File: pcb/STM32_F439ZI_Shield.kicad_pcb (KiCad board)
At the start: 2 copper layers, 70 x 133.4 mm, 112 parts, among them CN10 Conn_02x17_Odd_Even, CN7 Conn_02x10_Odd_Even, CN8 Conn_02x08_Odd_Even, CN9 Conn_02x15_Odd_Even, J1 Conn_01x02_Pin, J3 Relais_Conn, J4 Conn_01x02_Pin, J5 Conn_01x02_Pin, J6 Conn_01x02_Pin, J7 Conn_01x02_Pin, J8 Conn_01x02_Pin, K1 G6S-2, K2 G6S-2, U1 LM2904, U10 LTV-817S, U11 LTV-817S, U13 R-78E-5.0-1.0, U15 ACS724xLCTR-05AB, U2 MAX3485, U3 LTV-817S, U4 LTV-817S, U5 LTV-817S, U6 LTV-817S, U7 LTV-817S, U8 LTV-817S, U9 LTV-817S

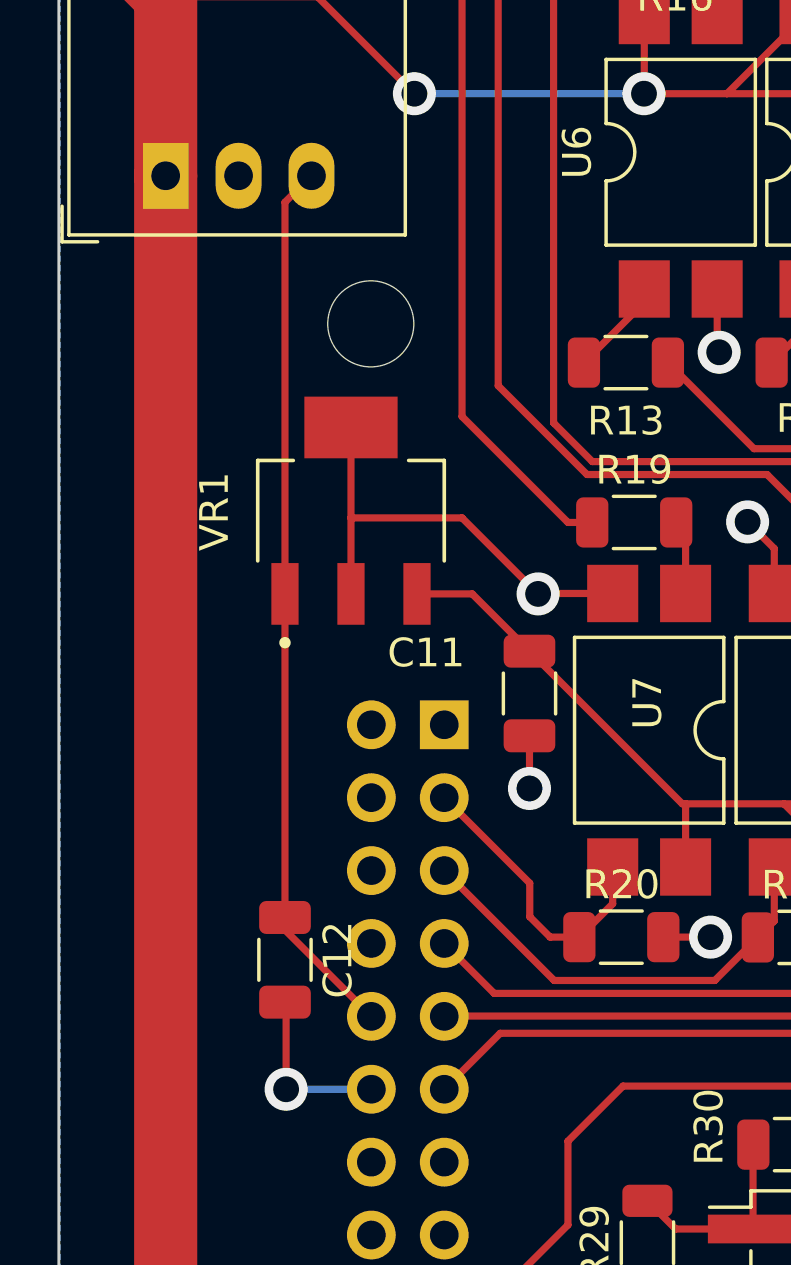
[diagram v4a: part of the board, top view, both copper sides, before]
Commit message: adjusted capacitor position
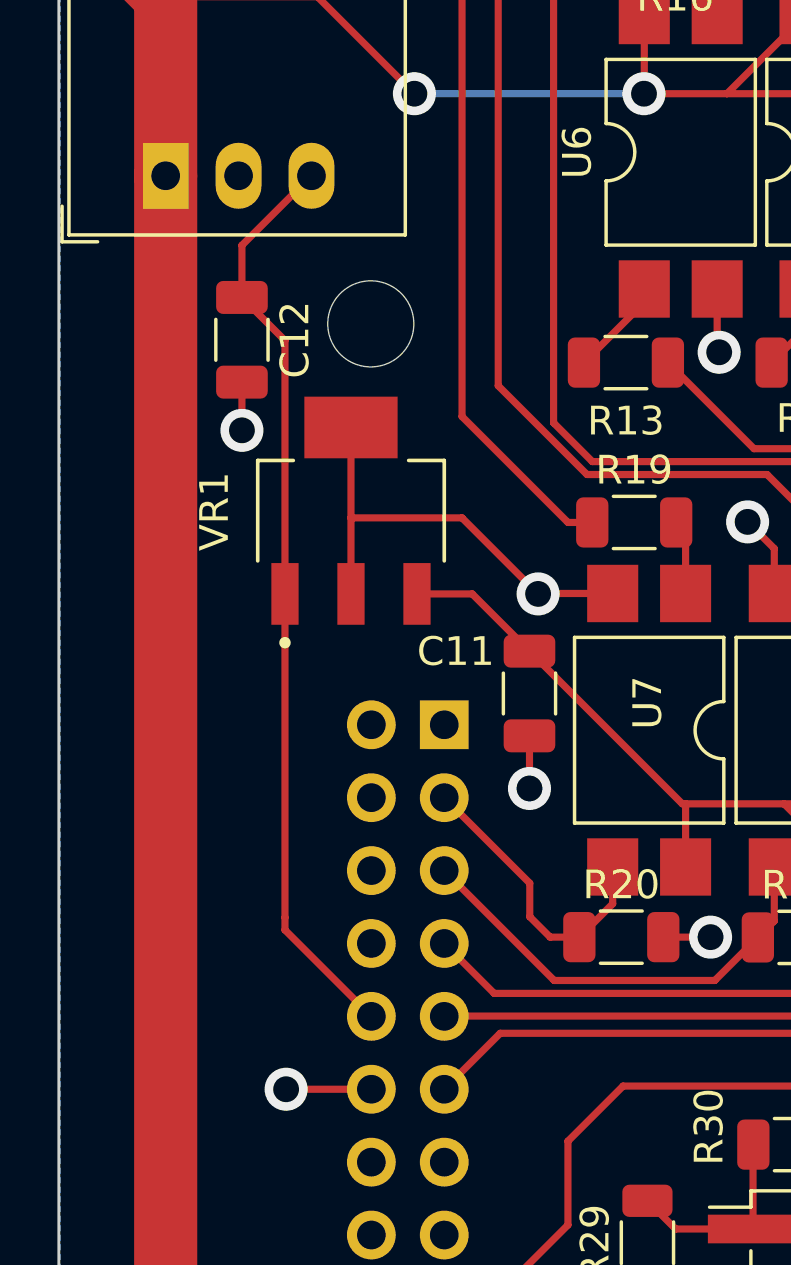
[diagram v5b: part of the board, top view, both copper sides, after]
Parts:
- moved C12 21.7 mm to (110.3, 52.5)
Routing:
- net GND: track 156.3 -> 154.9 mm, vias 42 -> 43
- net +5V: track 30.9 -> 32.2 mm
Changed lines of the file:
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@@
     )
   )
+  (footprint "Capacitor_SMD:C_1206_3216Metric" (layer "F.Cu")
+    (at 110.33 52.545 -90)
+    (descr "Capacitor SMD 1206 (3216 Metric), square (rectangular) end terminal, IPC_7351 nominal, (Body size source: IPC-SM-782 page 76, https://www.pcb-3d.com/wordpress/wp-content/uploads/ipc-sm-782a_amendment_1_and_2.pdf), generated with kicad-footprint-generator")
+    (tags "capacitor")
+    (property "Sheetfile" "STM32_F439ZI_Shield.kicad_sch")
+    (property "Sheetname" "")
+    (property "ki_description" "Unpolarized capacitor, small symbol")
+    (property "ki_keywords" "capacitor cap")
+    (attr smd)
+    (fp_text reference "C12" (at 0 -1.85 90) (layer "F.SilkS")
+        (effects (font (size 1 1) (thickness 0.15)))
+    )
+    (fp_text value "0.47uF" (at 0 1.85 90) (layer "F.Fab")
+        (effects (font (size 1 1) (thickness 0.15)))
+    )
+    (fp_text user "${REFERENCE}" (at 0 0 90) (layer "F.Fab")
+        (effects (font (size 0.8 0.8) (thickness 0.12)))
+    )
+    (fp_line (start -0.711252 -0.91) (end 0.711252 -0.91)
+      (stroke (width 0.12) (type solid)) (layer "F.SilkS"))
+    (fp_line (start -0.711252 0.91) (end 0.711252 0.91)
+      (stroke (width 0.12) (type solid)) (layer "F.SilkS"))
+    (fp_line (start -2.3 -1.15) (end 2.3 -1.15)
+      (stroke (width 0.05) (type solid)) (layer "F.CrtYd"))
+    (fp_line (start -2.3 1.15) (end -2.3 -1.15)
+      (stroke (width 0.05) (type solid)) (layer "F.CrtYd"))
+    (fp_line (start 2.3 -1.15) (end 2.3 1.15)
+      (stroke (width 0.05) (type solid)) (layer "F.CrtYd"))
+    (fp_line (start 2.3 1.15) (end -2.3 1.15)
+      (stroke (width 0.05) (type solid)) (layer "F.CrtYd"))
+    (fp_line (start -1.6 -0.8) (end 1.6 -0.8)
+      (stroke (width 0.1) (type solid)) (layer "F.Fab"))
+    (fp_line (start -1.6 0.8) (end -1.6 -0.8)
+      (stroke (width 0.1) (type solid)) (layer "F.Fab"))
+    (fp_line (start 1.6 -0.8) (end 1.6 0.8)
+      (stroke (width 0.1) (type solid)) (layer "F.Fab"))
+    (fp_line (start 1.6 0.8) (end -1.6 0.8)
+      (stroke (width 0.1) (type solid)) (layer "F.Fab"))
+    (pad "1" smd roundrect (at -1.475 0 270) (size 1.15 1.8) (layers "F.Cu" "F.Paste" "F.Mask") (roundrect_rratio 0.217391)
+      (net 148 "+5V") (pintype "passive"))
+    (pad "2" smd roundrect (at 1.475 0 270) (size 1.15 1.8) (layers "F.Cu" "F.Paste" "F.Mask") (roundrect_rratio 0.217391)
+      (net 2 "GND") (pintype "passive"))
+    (model "${KICAD6_3DMODEL_DIR}/Capacitor_SMD.3dshapes/C_1206_3216Metric.wrl"
+      (offset (xyz 0 0 0))
+      (scale (xyz 1 1 1))
+      (rotate (xyz 0 0 0))
+    )
+  )
   (footprint "Resistor_SMD:R_1206_3216Metric" (layer "F.Cu")
     (at 120.1 131.12 180)
@@
     (property "ki_keywords" "capacitor cap")
     (attr smd)
-    (fp_text reference "C11" (at -1.41 3.6) (layer "F.SilkS")
+    (fp_text reference "C11" (at -1.46 2.57) (layer "F.SilkS")
         (effects (font (size 1 1) (thickness 0.15)))
     )
@@
     )
   )
-  (footprint "Capacitor_SMD:C_1206_3216Metric" (layer "F.Cu")
-    (at 111.83 74.15 -90)
-    (descr "Capacitor SMD 1206 (3216 Metric), square (rectangular) end terminal, IPC_7351 nominal, (Body size source: IPC-SM-782 page 76, https://www.pcb-3d.com/wordpress/wp-content/uploads/ipc-sm-782a_amendment_1_and_2.pdf), generated with kicad-footprint-generator")
-    (tags "capacitor")
-    (property "Sheetfile" "STM32_F439ZI_Shield.kicad_sch")
-    (property "Sheetname" "")
-    (property "ki_description" "Unpolarized capacitor, small symbol")
-    (property "ki_keywords" "capacitor cap")
-    (attr smd)
-    (fp_text reference "C12" (at 0 -1.85 90) (layer "F.SilkS")
-        (effects (font (size 1 1) (thickness 0.15)))
-    )
-    (fp_text value "0.47uF" (at 0 1.85 90) (layer "F.Fab")
-        (effects (font (size 1 1) (thickness 0.15)))
-    )
-    (fp_text user "${REFERENCE}" (at 0 0 90) (layer "F.Fab")
-        (effects (font (size 0.8 0.8) (thickness 0.12)))
-    )
-    (fp_line (start -0.711252 -0.91) (end 0.711252 -0.91)
-      (stroke (width 0.12) (type solid)) (layer "F.SilkS"))
-    (fp_line (start -0.711252 0.91) (end 0.711252 0.91)
-      (stroke (width 0.12) (type solid)) (layer "F.SilkS"))
-    (fp_line (start -2.3 -1.15) (end 2.3 -1.15)
-      (stroke (width 0.05) (type solid)) (layer "F.CrtYd"))
-    (fp_line (start -2.3 1.15) (end -2.3 -1.15)
-      (stroke (width 0.05) (type solid)) (layer "F.CrtYd"))
-    (fp_line (start 2.3 -1.15) (end 2.3 1.15)
-      (stroke (width 0.05) (type solid)) (layer "F.CrtYd"))
-    (fp_line (start 2.3 1.15) (end -2.3 1.15)
-      (stroke (width 0.05) (type solid)) (layer "F.CrtYd"))
-    (fp_line (start -1.6 -0.8) (end 1.6 -0.8)
-      (stroke (width 0.1) (type solid)) (layer "F.Fab"))
-    (fp_line (start -1.6 0.8) (end -1.6 -0.8)
-      (stroke (width 0.1) (type solid)) (layer "F.Fab"))
-    (fp_line (start 1.6 -0.8) (end 1.6 0.8)
-      (stroke (width 0.1) (type solid)) (layer "F.Fab"))
-    (fp_line (start 1.6 0.8) (end -1.6 0.8)
-      (stroke (width 0.1) (type solid)) (layer "F.Fab"))
-    (pad "1" smd roundrect (at -1.475 0 270) (size 1.15 1.8) (layers "F.Cu" "F.Paste" "F.Mask") (roundrect_rratio 0.217391)
-      (net 148 "+5V") (pintype "passive"))
-    (pad "2" smd roundrect (at 1.475 0 270) (size 1.15 1.8) (layers "F.Cu" "F.Paste" "F.Mask") (roundrect_rratio 0.217391)
-      (net 2 "GND") (pintype "passive"))
-    (model "${KICAD6_3DMODEL_DIR}/Capacitor_SMD.3dshapes/C_1206_3216Metric.wrl"
-      (offset (xyz 0 0 0))
-      (scale (xyz 1 1 1))
-      (rotate (xyz 0 0 0))
-    )
-  )
   (footprint "LED_SMD:LED_1206_3216Metric" (layer "F.Cu")
     (at 168.7 91.06 180)
@@
   (segment (start 146.98 74.395) (end 149.1775 74.395) (width 0.25) (layer "F.Cu") (net 2))
   (segment (start 125.0125 73.36) (end 126.66 73.36) (width 0.25) (layer "F.Cu") (net 2))
+  (segment (start 110.33 54.02) (end 110.33 55.7) (width 0.25) (layer "F.Cu") (net 2))
   (segment (start 122.030353 35.639647) (end 122.3 35.37) (width 0.25) (layer "F.Cu") (net 2))
   (segment (start 118 58.75) (end 120.65 61.4) (width 0.25) (layer "F.Cu") (net 2))
@@
   (segment (start 140.56 36.84) (end 140.56 38.5625) (width 0.25) (layer "F.Cu") (net 2))
   (segment (start 128.64 144.54) (end 128.64 142.83) (width 0.25) (layer "F.Cu") (net 2))
+  (segment (start 114.84 78.66) (end 111.87 78.66) (width 0.25) (layer "F.Cu") (net 2))
   (segment (start 114.13 61.4) (end 114.13 58.75) (width 0.25) (layer "F.Cu") (net 2))
   (segment (start 130.14 144.54) (end 130.305 144.375) (width 0.25) (layer "F.Cu") (net 2))
   (segment (start 148.44 100.39) (end 148.44 98.49) (width 0.25) (layer "F.Cu") (net 2))
-  (segment (start 111.87 78.66) (end 111.87 75.665) (width 0.25) (layer "F.Cu") (net 2))
   (segment (start 139.22 73.36) (end 137.4425 73.36) (width 0.25) (layer "F.Cu") (net 2))
   (segment (start 155.11 124.7725) (end 155.11 125.46) (width 0.25) (layer "F.Cu") (net 2))
@@
   (segment (start 173.08 148.93) (end 171.4075 148.93) (width 0.25) (layer "F.Cu") (net 2))
   (segment (start 129.57 35.55) (end 128.2 36.92) (width 0.25) (layer "F.Cu") (net 2))
-  (segment (start 111.87 75.665) (end 111.83 75.625) (width 0.25) (layer "F.Cu") (net 2))
   (segment (start 129.57 35.3825) (end 129.57 35.55) (width 0.25) (layer "F.Cu") (net 2))
   (segment (start 155.11 125.46) (end 156.21 126.56) (width 0.25) (layer "F.Cu") (net 2))
@@
   (via (at 162.96 32.54) (size 1.5) (drill 0.9) (layers "F.Cu" "B.Cu") (net 2))
   (via (at 135.01 58.87) (size 1.5) (drill 0.9) (layers "F.Cu" "B.Cu") (net 2))
+  (via (at 110.33 55.7) (size 1.5) (drill 0.9) (layers "F.Cu" "B.Cu") (free) (net 2))
   (via (at 172.41 91.06) (size 1.5) (drill 0.9) (layers "F.Cu" "B.Cu") (net 2))
   (via (at 172.56 32.91) (size 1.5) (drill 0.9) (layers "F.Cu" "B.Cu") (net 2))
@@
   (via (at 125.14 36.86) (size 1.5) (drill 0.9) (layers "F.Cu" "B.Cu") (net 2))
   (via (at 127.95 58.89) (size 1.5) (drill 0.9) (layers "F.Cu" "B.Cu") (net 2))
-  (segment (start 111.87 78.66) (end 114.84 78.66) (width 0.25) (layer "B.Cu") (net 2))
   (segment (start 157.455 119.31) (end 160.47 119.31) (width 0.25) (layer "F.Cu") (net 3))
   (segment (start 141.95 129.93) (end 152.56 119.32) (width 0.25) (layer "F.Cu") (net 3))
@@
   (segment (start 128.14 83.53) (end 128.14 80.6) (width 0.25) (layer "F.Cu") (net 147))
   (segment (start 125.4425 83.53) (end 128.14 83.53) (width 0.25) (layer "F.Cu") (net 147))
-  (segment (start 112.753 46.83) (end 111.83 47.753) (width 0.25) (layer "F.Cu") (net 148))
+  (segment (start 112.753 46.83) (end 110.33 49.253) (width 0.25) (layer "F.Cu") (net 148))
+  (segment (start 111.83 52.57) (end 111.83 61.4) (width 0.25) (layer "F.Cu") (net 148))
+  (segment (start 110.33 49.253) (end 110.33 51.07) (width 0.25) (layer "F.Cu") (net 148))
   (segment (start 111.83 73.11) (end 114.84 76.12) (width 0.25) (layer "F.Cu") (net 148))
+  (segment (start 110.33 51.07) (end 111.83 52.57) (width 0.25) (layer "F.Cu") (net 148))
   (segment (start 111.83 72.675) (end 111.83 73.11) (width 0.25) (layer "F.Cu") (net 148))
   (segment (start 111.83 72.675) (end 111.83 61.4) (width 0.25) (layer "F.Cu") (net 148))
-  (segment (start 111.83 47.753) (end 111.83 61.4) (width 0.25) (layer "F.Cu") (net 148))
   (zone (net 2) (net_name "GND") (layer "B.Cu") (hatch edge 0.5)
     (connect_pads (clearance 0.5))

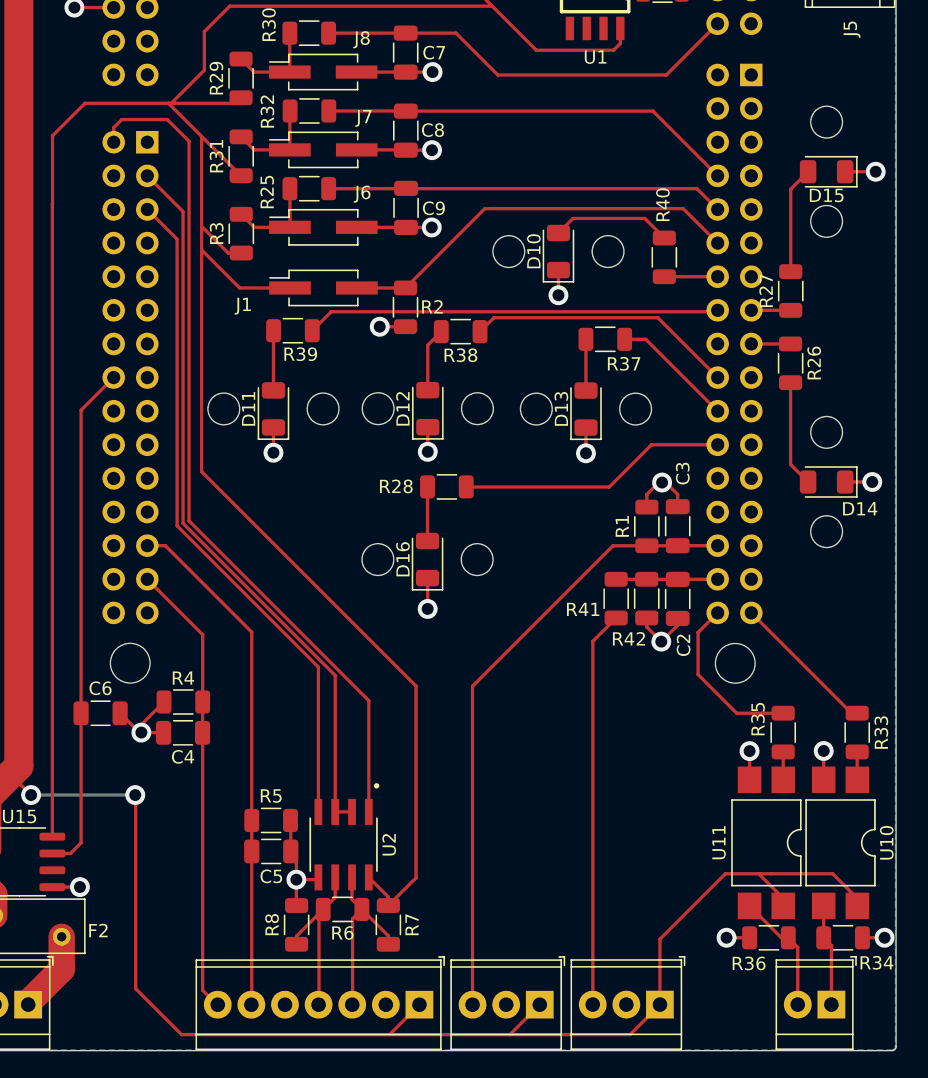
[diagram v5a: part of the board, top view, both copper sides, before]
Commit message: updated pcb and assigned correct pins
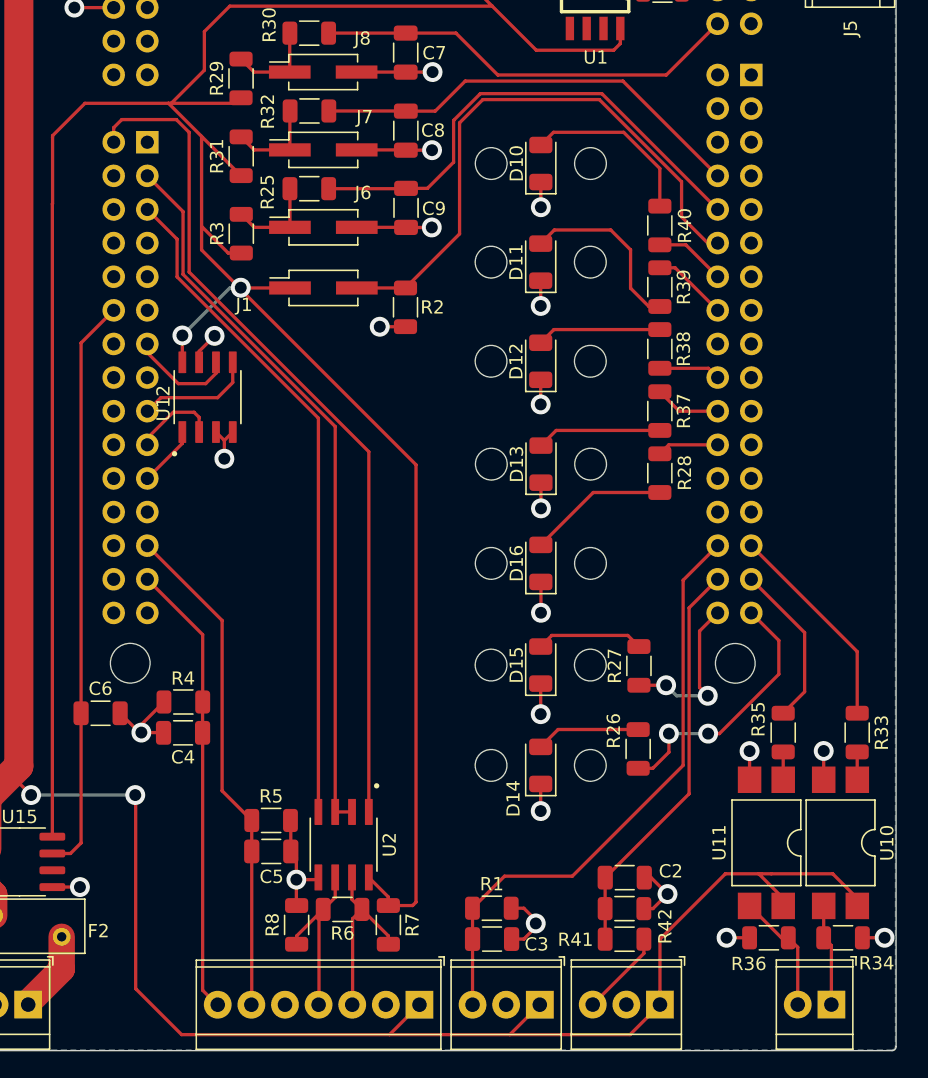
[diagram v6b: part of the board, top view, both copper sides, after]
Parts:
- added U12: FL25L16B, SOIC127P602X172-8N:SOIC127P602X172-8N, F.Cu at (121.9, 108.1)
- moved D15 43.1 mm to (147.1, 128.3), turned to 90 degrees
- moved C3 34.2 mm to (143.4, 149.0), turned to 0 degrees
- moved R26 31.3 mm to (154.5, 134.7), turned to 90 degrees
- moved R1 31.1 mm to (143.4, 146.7), turned to 0 degrees
- moved R27 30.6 mm to (154.5, 128.4)
- moved D14 30.4 mm to (147.1, 135.9), turned to 90 degrees
- moved R39 27.9 mm to (156.1, 99.8), turned to -90 degrees
- moved R41 25.7 mm to (153.4, 149.0), turned to 0 degrees
- moved R42 23.5 mm to (153.4, 146.7), turned to 0 degrees
- moved D11 23.0 mm to (147.1, 97.9)
- moved C2 21.4 mm to (153.4, 144.4), turned to 0 degrees
- moved R28 16.1 mm to (156.1, 113.8), turned to -90 degrees
- moved R38 15.1 mm to (156.1, 104.4), turned to 90 degrees
- moved D12 9.25 mm to (147.1, 105.4)
- moved D16 8.56 mm to (147.1, 120.7)
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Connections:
- CN10 pad 15: /Buttons_LEDS/MCU_LED_Rollen -> unconnected-(CN10-Pin_15-Pad15)
- CN10 pad 17: /Buttons_LEDS/MCU_LED_Trimmen -> unconnected-(CN10-Pin_17-Pad17)
- CN10 pad 29: unconnected-(CN10-Pin_29-Pad29) -> /Optokoppler/Ext_Relais1_MCU
- CN10 pad 31: unconnected-(CN10-Pin_31-Pad31) -> /Optokoppler/Ext_Relais2_MCU
- CN10 pad 33: /Optokoppler/Ext_Relais1_MCU -> /Buttons_LEDS/MCU_LED_Trimmen
- CN10 pad 34: /Optokoppler/Ext_Relais2_MCU -> /Buttons_LEDS/MCU_LED_Rollen
- CN9 pad 12: unconnected-(CN9-Pin_12-Pad12) -> /Motor/Stromsensor_MCU
- CN9 pad 13: unconnected-(CN9-Pin_13-Pad13) -> /STM32F439ZI/SCK
- CN9 pad 16: /Motor/Stromsensor_MCU -> unconnected-(CN9-Pin_16-Pad16)
- CN9 pad 17: unconnected-(CN9-Pin_17-Pad17) -> /STM32F439ZI/MISO
- CN9 pad 19: unconnected-(CN9-Pin_19-Pad19) -> /STM32F439ZI/MOSI
- CN9 pad 21: unconnected-(CN9-Pin_21-Pad21) -> /STM32F439ZI/CS
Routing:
- net /Buttons_LEDS/MCU_LED_Betrieb: track 31.3 -> 5.70 mm
- net Net-(Kraftmessung1-Pin_3): track 30.0 -> 6.54 mm
- net /STM32F439ZI/Kraftmessung_MCU: track 7.68 -> 30.7 mm
- net /Buttons_LEDS/MCU_LED_Trimmen: track 2.97 -> 19.9 mm, vias 0 -> 2
- net /Buttons_LEDS/MCU_LED_Kalibrierung: track 20.3 -> 4.65 mm
- net /Buttons_LEDS/MCU_LED_Manuell: track 20.3 -> 4.66 mm
- net /Buttons_LEDS/MCU_Switch: track 30.8 -> 44.1 mm
- net /Buttons_LEDS/MCU_LED_Rollen: track 2.98 -> 12.6 mm, vias 0 -> 2
- net Net-(D11-A): track 4.51 -> 13.5 mm
- net /STM32F439ZI/MISO: track 0.00 -> 8.88 mm
- net /STM32F439ZI/SCK: track 0.00 -> 7.98 mm
- net /Buttons_LEDS/MCU_Kalibrierung: track 30.1 -> 37.8 mm
- net Net-(D16-A): track 4.09 -> 10.6 mm
- net /STM32F439ZI/MOSI: track 0.00 -> 6.50 mm
- net GND: track 154.9 -> 160.6 mm, vias 43 -> 45
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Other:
- outline, holes or cut-outs redrawn
